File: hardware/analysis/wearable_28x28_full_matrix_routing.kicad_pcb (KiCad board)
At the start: 4 copper layers, 61.2 x 61.2 mm, 784 parts

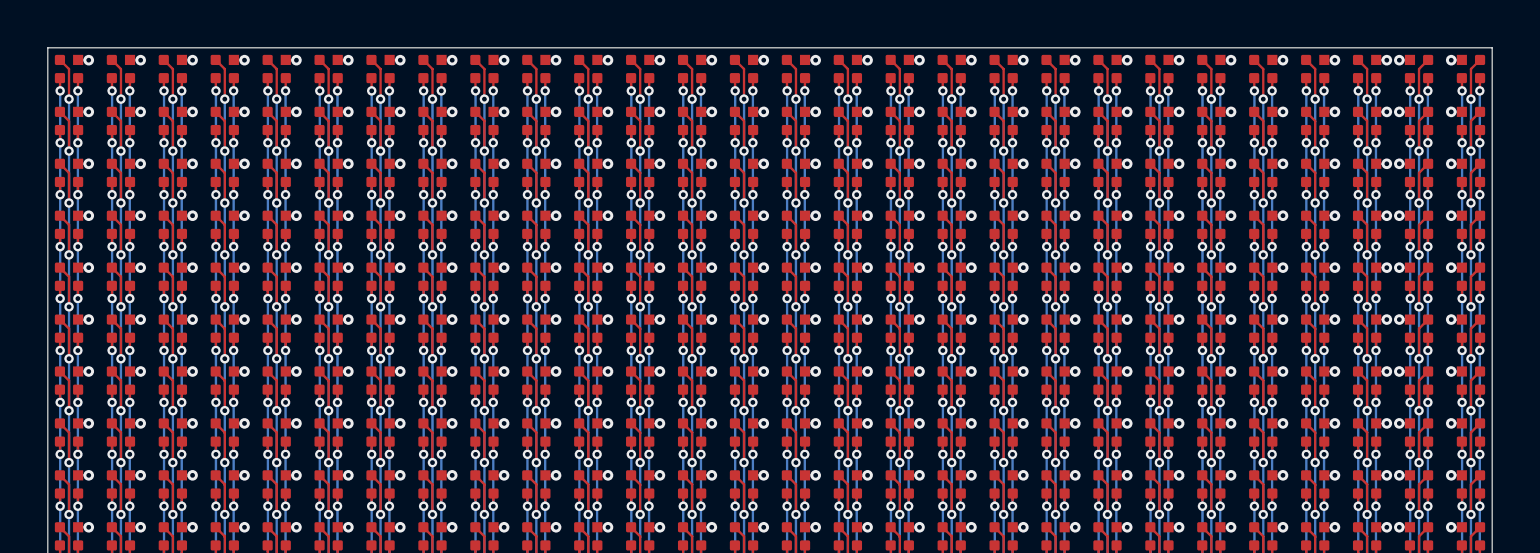
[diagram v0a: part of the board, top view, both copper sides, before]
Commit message: Place 20x20 backside parts outside the via field
Co-authored-by: illiapliukhin <illiapliukhin@users.noreply.github.com>
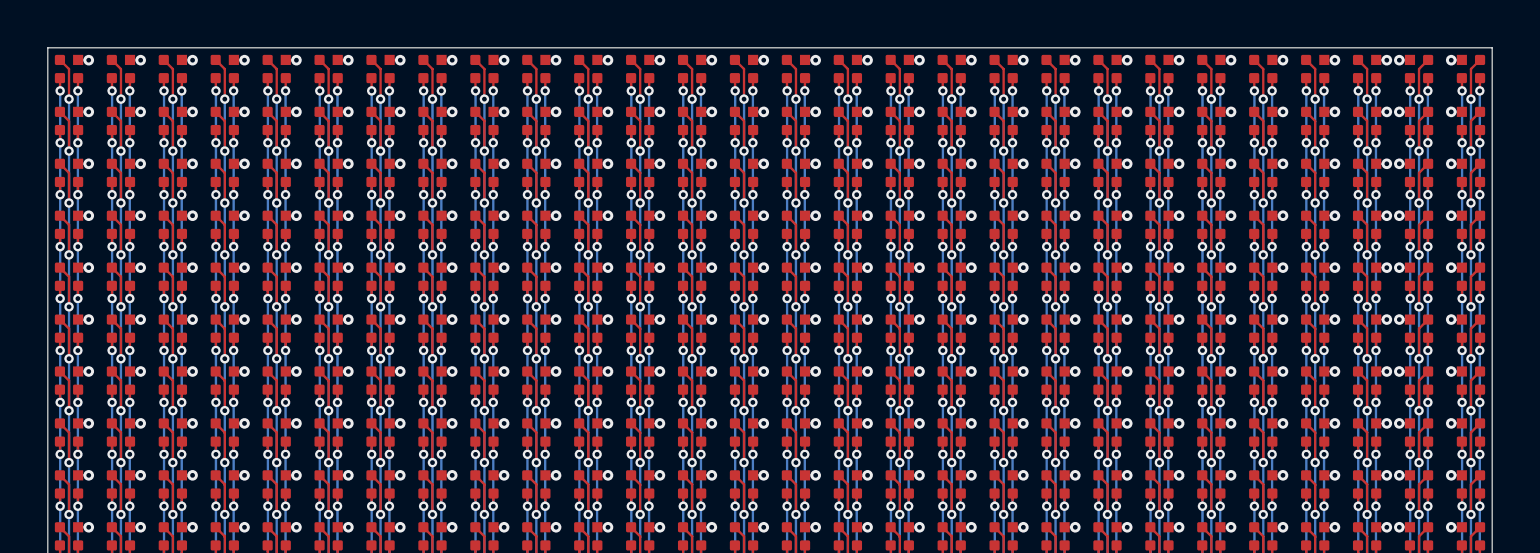
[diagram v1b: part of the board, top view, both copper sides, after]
